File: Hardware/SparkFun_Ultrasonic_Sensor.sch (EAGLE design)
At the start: 67 parts, among them J4 Vertical Qwiic Connector, J6 Vertical Qwiic Connector, Q1 600mA/40V, U5 ULTRASONIC_SENSOR_TRANSMITTER, U6 LMV324, U7 STM8L051F3, U8 SP3232EB, U9 ULTRASONIC_SENSOR_RECEIVER

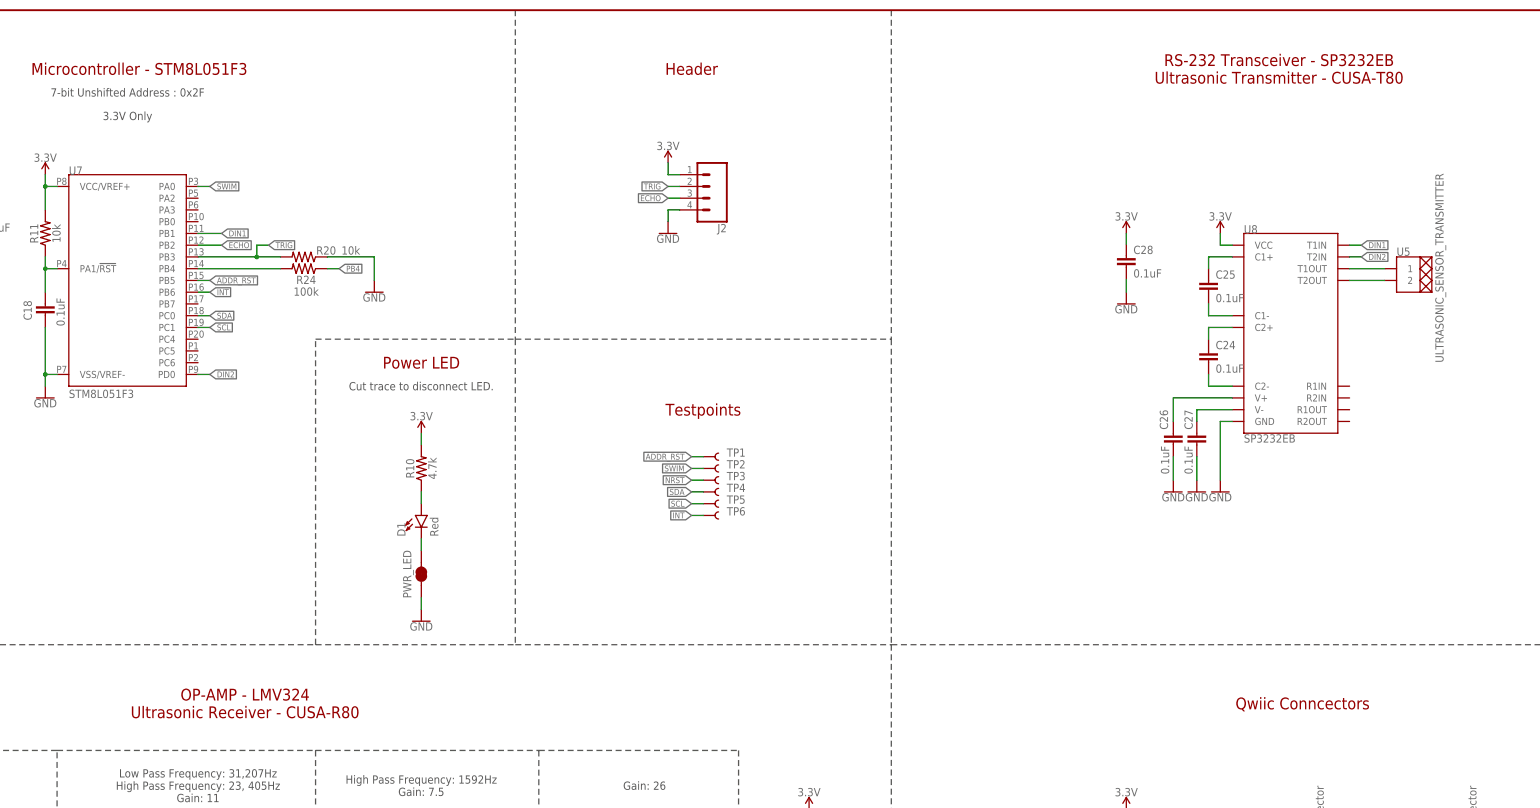
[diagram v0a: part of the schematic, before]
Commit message: Updates the board files with the new part names
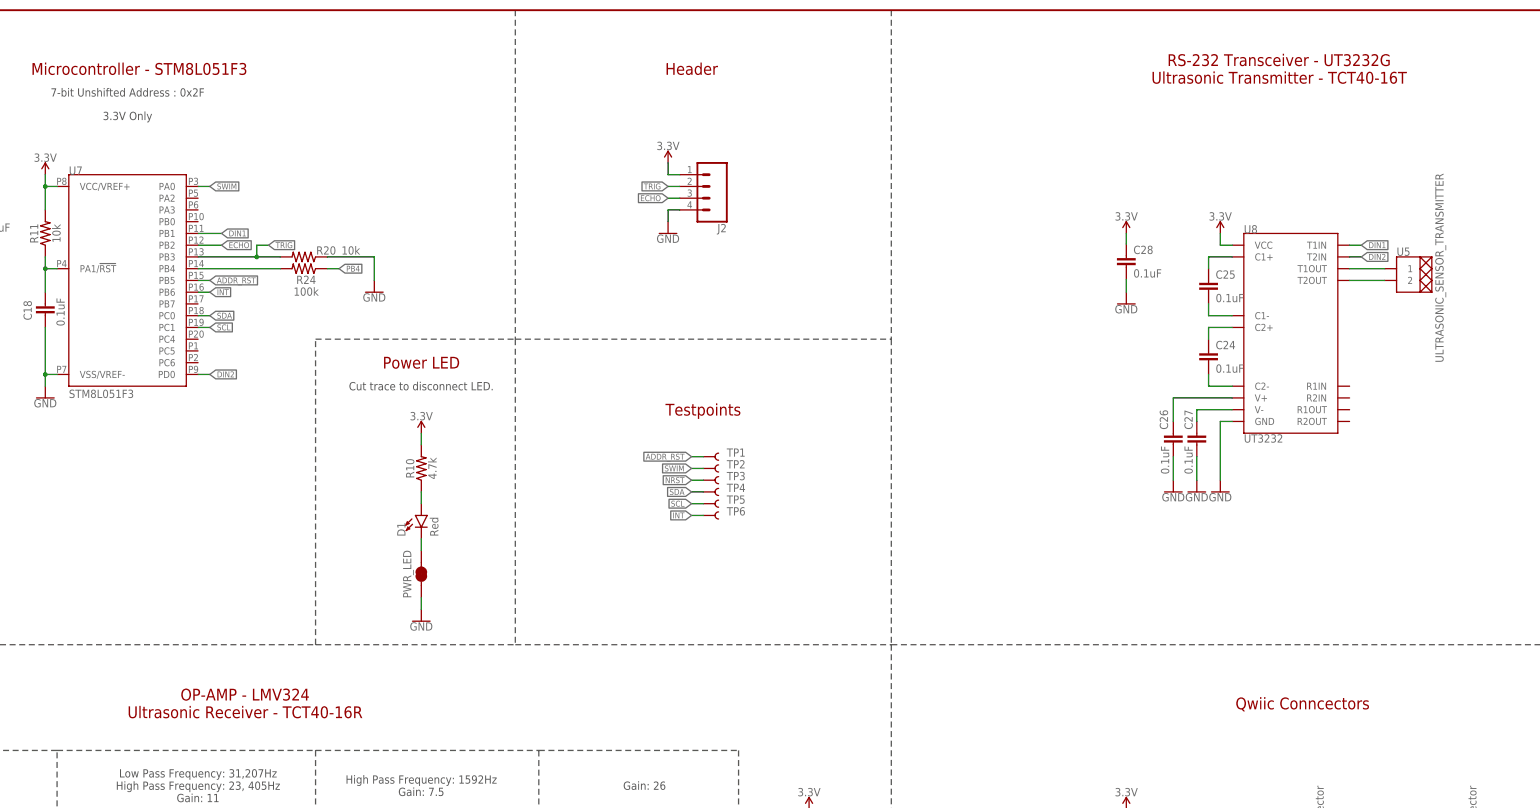
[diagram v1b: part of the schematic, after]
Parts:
- U8: value SP3232EB -> UT3232; device new_parts:SP3232EB -> new_parts:UT3232
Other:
- note added: "OP-AMP - LMV324 Ultrasonic Receiver - TCT40-16R"
- note added: "RS-232 Transceiver - UT3232G Ultrasonic Transmitter - TCT40-16T"
- note removed: "OP-AMP - LMV324 Ultrasonic Receiver - CUSA-R80"
- note removed: "RS-232 Transceiver - SP3232EB Ultrasonic Transmitter - CUSA-T80"
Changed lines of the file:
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@@
 <part name="GND18" library="SparkFun-PowerSymbols" deviceset="GND" device=""/>
 <part name="TP1" library="SparkFun-Connectors" deviceset="TEST-POINT" device="3X5" value="TEST-POINT3X5"/>
-<part name="U8" library="new_parts" deviceset="SP3232EB" device=""/>
+<part name="U8" library="new_parts" deviceset="UT3232" device=""/>
 <part name="FRAME1" library="SparkFun-Aesthetics" deviceset="FRAME-LEDGER" device="">
 <attribute name="DESIGNER" value="NOA Labs"/>
@@
 <text x="96.52" y="266.7" size="2.54" layer="94" font="vector" align="center">Microcontroller - STM8L051F3</text>
 <text x="218.44" y="193.04" size="2.54" layer="94" font="vector" align="center">Testpoints</text>
-<text x="342.9" y="266.7" size="2.54" layer="94" font="vector" align="center">RS-232 Transceiver - SP3232EB
-Ultrasonic Transmitter - CUSA-T80</text>
+<text x="342.9" y="266.7" size="2.54" layer="94" font="vector" align="center">RS-232 Transceiver - UT3232G
+Ultrasonic Transmitter - TCT40-16T</text>
 <text x="119.38" y="129.54" size="2.54" layer="94" font="vector" align="center">OP-AMP - LMV324
-Ultrasonic Receiver - CUSA-R80</text>
+Ultrasonic Receiver - TCT40-16R</text>
 <text x="347.98" y="129.54" size="2.54" layer="94" font="vector" align="center">Qwiic Conncectors</text>
 <text x="215.9" y="266.7" size="2.54" layer="94" font="vector" align="center">Header</text>

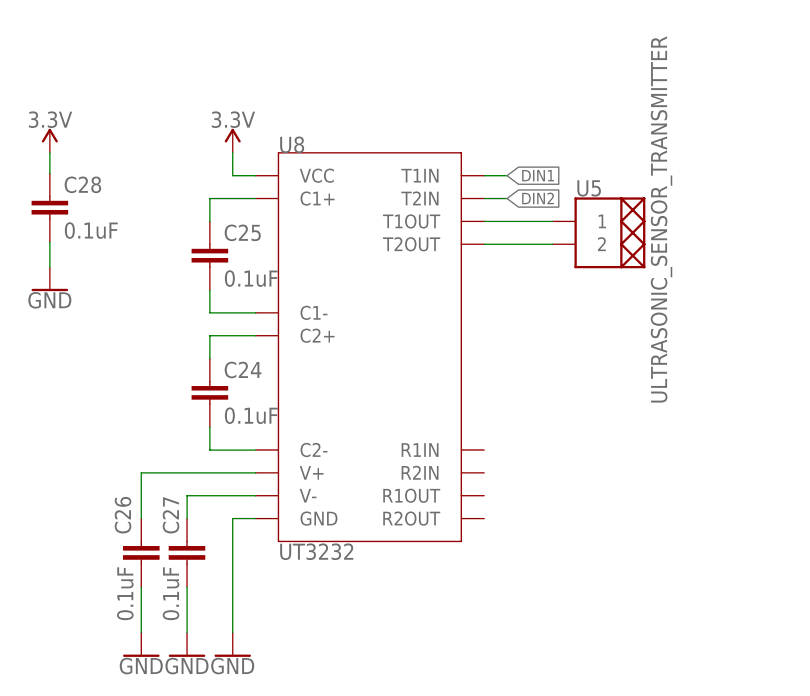
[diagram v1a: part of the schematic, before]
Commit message: Removes old hex file, updates design with correct pin names on RS-232 transceiver
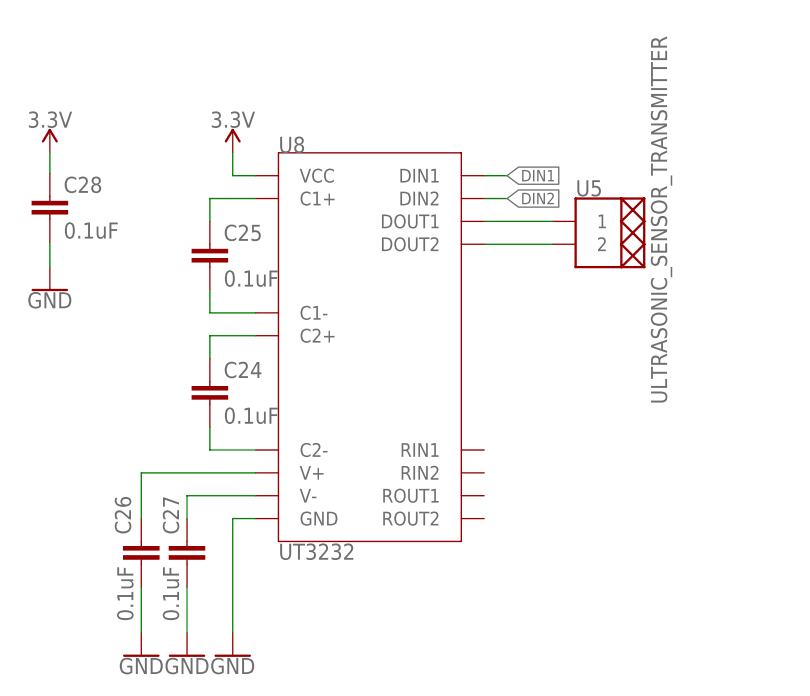
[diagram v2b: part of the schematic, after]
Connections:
- net DIN1: now also U8.DIN1; no longer U8.T1IN
- net DIN2: now also U8.DIN2; no longer U8.T2IN
- net N$48: now also U8.DOUT1; no longer U8.T1OUT
- net N$49: now also U8.DOUT2; no longer U8.T2OUT
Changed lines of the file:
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@@
 </segment>
 <segment>
-<pinref part="U8" gate="G$1" pin="T2IN"/>
+<pinref part="U8" gate="G$1" pin="DIN2"/>
 <wire x1="360.68" y1="226.06" x2="358.14" y2="226.06" width="0.1524" layer="91"/>
 <label x="360.68" y="226.06" size="1.27" layer="95" font="vector" xref="yes"/>
@@
 </segment>
 <segment>
-<pinref part="U8" gate="G$1" pin="T1IN"/>
+<pinref part="U8" gate="G$1" pin="DIN1"/>
 <wire x1="360.68" y1="228.6" x2="358.14" y2="228.6" width="0.1524" layer="91"/>
 <label x="360.68" y="228.6" size="1.27" layer="95" font="vector" xref="yes"/>
@@
 <net name="N$48" class="0">
 <segment>
-<pinref part="U8" gate="G$1" pin="T1OUT"/>
+<pinref part="U8" gate="G$1" pin="DOUT1"/>
 <wire x1="365.76" y1="223.52" x2="358.14" y2="223.52" width="0.1524" layer="91"/>
 <pinref part="U5" gate="G$1" pin="1"/>
@@
 <net name="N$49" class="0">
 <segment>
-<pinref part="U8" gate="G$1" pin="T2OUT"/>
+<pinref part="U8" gate="G$1" pin="DOUT2"/>
 <wire x1="365.76" y1="220.98" x2="358.14" y2="220.98" width="0.1524" layer="91"/>
 <pinref part="U5" gate="G$1" pin="2"/>
